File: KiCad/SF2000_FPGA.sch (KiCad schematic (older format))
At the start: 20 parts, among them J10 Conn_02x01, J11 Conn_02x01, J12 Conn_01x01, J13 Conn_02x01, J3 Conn_02x03_Odd_Even, J4 Conn_02x01, J8 Conn_02x01, J9 Conn_02x01, U3 74LVC2G14, U7 10M04SCE144

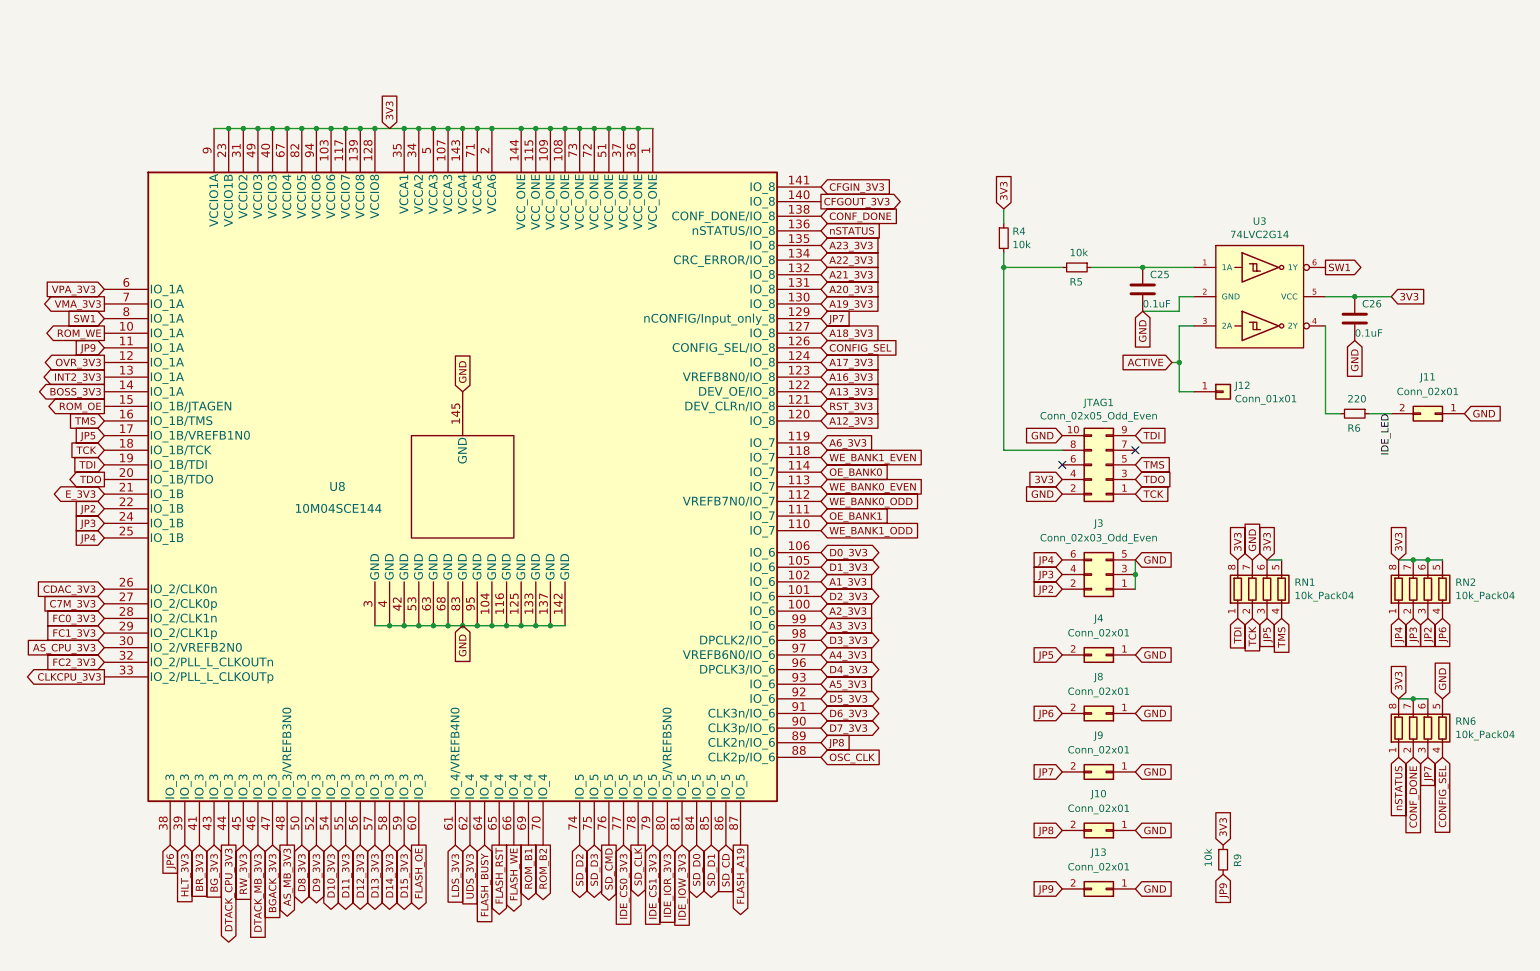
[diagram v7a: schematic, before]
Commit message: Re-routed for a GoWin FPGA GW1N-UV9LQ144 (or GW1N-UV4LQ144) and added a Pmod type 2A SPI-header.
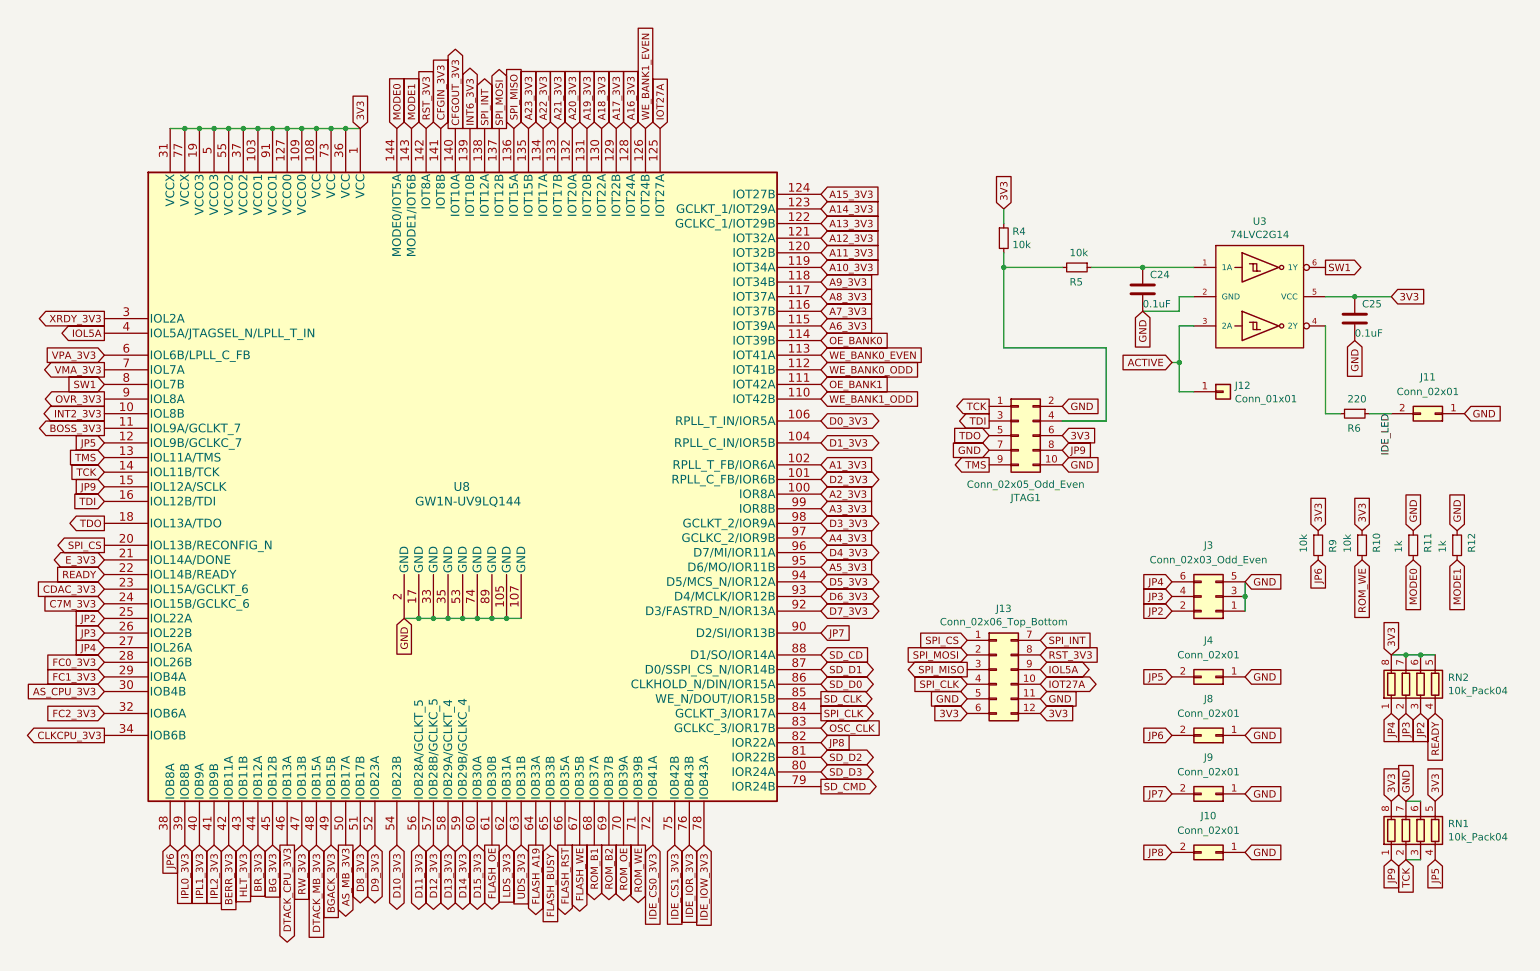
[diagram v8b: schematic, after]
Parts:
- removed J13: Conn_02x01, Connector_PinHeader_2.00mm:PinHeader_2x01_P2.00mm_Vertical, symbol Connector_Generic:Conn_02x01
- removed RN6: 10k_Pack04, SF2000:RESCAF80P320X160X60-8N, symbol Device:R_Pack04
- removed U7: 10M04SCE144, SF2000:EQFP-144-1EP_20x20mm_P0.5mm_EP5x5mm_TH_GND_pad, symbol SF2000:10M04SCE144
- added J13: Conn_02x06_Top_Bottom, SF2000:Pmod_Interface_Type_2A_SPI_PinSocket_2x06_P2.54mm_Horizontal, symbol Connector_Generic:Conn_02x06_Top_Bottom
- added R10: 10k, Resistor_SMD:R_0805_2012Metric_Pad1.15x1.40mm_HandSolder, symbol Device:R_Small
- added R11, R12: 1k, Resistor_SMD:R_0805_2012Metric_Pad1.15x1.40mm_HandSolder, symbol Device:R_Small
- added U8: GW1N-UV9LQ144, Package_QFP:LQFP-144_20x20mm_P0.5mm, symbol SF2000:GW1N-UV9LQ144
- renumbered C25 to C24, C26 to C25
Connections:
- net 3V3: now also JTAG1.6 (Pin_6), J13.12 (Pin_12), J13.6 (Pin_6), R10.1, U8.1 (VCC), U8.103 (VCCO1), U8.108 (VCC), U8.109 (VCCO0), U8.127 (VCCO0), U8.19 (VCCO3), U8.31 (VCCX), U8.36 (VCC), U8.37 (VCCO2), U8.5 (VCCO3), U8.55 (VCCO2), U8.73 (VCC), U8.77 (VCCX), U8.91 (VCCO1); no longer JTAG1.4 (Pin_4), RN1.6 (R3.2)
- net A12_3V3: now also U8.121 (IOT32A)
- net A13_3V3: now also U8.122 (GCLKC_1/IOT29B)
- net A16_3V3: now also U8.128 (IOT24A)
- net A17_3V3: now also U8.129 (IOT22B)
- net A18_3V3: now also U8.130 (IOT22A)
- net A19_3V3: now also U8.131 (IOT20B)
- net A1_3V3: now also U8.102 (RPLL_T_FB/IOR6A)
- net A20_3V3: now also U8.132 (IOT20A)
- net A21_3V3: now also U8.133 (IOT17B)
- net A22_3V3: now also U8.134 (IOT17A)
- net A23_3V3: now also U8.135 (IOT15B)
- net A2_3V3: now also U8.100 (IOR8A)
- net A3_3V3: now also U8.99 (IOR8B)
- net A4_3V3: now also U8.97 (GCLKC_2/IOR9B)
- net A5_3V3: now also U8.95 (D6/MO/IOR11B)
- net A6_3V3: now also U8.115 (IOT39A)
- net AS_CPU_3V3: now also U8.30 (IOB4B)
- net AS_MB_3V3: now also U8.50 (IOB17A)
- net BGACK_3V3: now also U8.49 (IOB15B)
- net BG_3V3: now also U8.45 (IOB12B)
- net BOSS_3V3: now also U8.11 (IOL9A/GCLKT_7)
- net BR_3V3: now also U8.44 (IOB12A)
- net C7M_3V3: now also U8.24 (IOL15B/GCLKC_6)
- net CDAC_3V3: now also U8.23 (IOL15A/GCLKT_6)
- net CFGIN_3V3: now also U8.141 (IOT8B)
- net CFGOUT_3V3: now also U8.140 (IOT10A)
- net CLKCPU_3V3: now also U8.34 (IOB6B)
- net D0_3V3: now also U8.106 (RPLL_T_IN/IOR5A)
- net D10_3V3: now also U8.54 (IOB23B)
- net D11_3V3: now also U8.56 (IOB28A/GCLKT_5)
- net D12_3V3: now also U8.57 (IOB28B/GCLKC_5)
- net D13_3V3: now also U8.58 (IOB29A/GCLKT_4)
- net D14_3V3: now also U8.59 (IOB29B/GCLKC_4)
- net D15_3V3: now also U8.60 (IOB30A)
- net D1_3V3: now also U8.104 (RPLL_C_IN/IOR5B)
- net D2_3V3: now also U8.101 (RPLL_C_FB/IOR6B)
- net D3_3V3: now also U8.98 (GCLKT_2/IOR9A)
- net D4_3V3: now also U8.96 (D7/MI/IOR11A)
- net D5_3V3: now also U8.94 (D5/MCS_N/IOR12A)
- net D6_3V3: now also U8.93 (D4/MCLK/IOR12B)
- net D7_3V3: now also U8.92 (D3/FASTRD_N/IOR13A)
- net D8_3V3: now also U8.51 (IOB17B)
- net D9_3V3: now also U8.52 (IOB23A)
- net DTACK_CPU_3V3: now also U8.46 (IOB13A)
- net DTACK_MB_3V3: now also U8.48 (IOB15A)
- net E_3V3: now also U8.21 (IOL14A/DONE)
- net FC0_3V3: now also U8.28 (IOL26B)
- net FC1_3V3: now also U8.29 (IOB4A)
- net FC2_3V3: now also U8.32 (IOB6A)
- net FLASH_A19: now also U8.64 (IOB33A)
- net FLASH_BUSY: now also U8.65 (IOB33B)
- net FLASH_OE: now also U8.61 (IOB30B)
- net FLASH_RST: now also U8.66 (IOB35A)
- net FLASH_WE: now also U8.67 (IOB35B)
- net GND: now also JTAG1.7 (Pin_7), RN1.6 (R3.2), J13.11 (Pin_11), J13.5 (Pin_5), R11.1, R12.1, U8.105 (GND), U8.107 (GND), U8.17 (GND), U8.2 (GND), U8.33 (GND), U8.35 (GND), U8.53 (GND), U8.74 (GND), U8.89 (GND)
- net HLT_3V3: now also U8.43 (IOB11B)
- net IDE_CS0_3V3: now also U8.72 (IOB41A)
- net IDE_CS1_3V3: now also U8.75 (IOB42B)
- net IDE_IOR_3V3: now also U8.76 (IOB43B)
- net IDE_IOW_3V3: now also U8.78 (IOB43A)
- net INT2_3V3: now also U8.10 (IOL8B)
- net JP2: now also U8.25 (IOL22A)
- net JP3: now also U8.26 (IOL22B)
- net JP4: now also U8.27 (IOL26A)
- net JP5: now also RN1.4 (R4.1), U8.12 (IOL9B/GCLKC_7); no longer RN1.3 (R3.1)
- net JP6: now also R9.2, U8.38 (IOB8A); no longer RN2.4 (R4.1)
- net JP7: now also U8.90 (D2/SI/IOR13B)
- net JP8: now also U8.82 (IOR22A)
- net JP9: now also JTAG1.8 (Pin_8), RN1.1 (R1.1), U8.15 (IOL12A/SCLK); no longer R9.2
- net LDS_3V3: now also U8.62 (IOB31A)
- net OE_BANK0: now also U8.114 (IOT39B)
- net OE_BANK1: now also U8.111 (IOT42A)
- net OSC_CLK: now also U8.83 (GCLKC_3/IOR17B)
- net OVR_3V3: now also U8.9 (IOL8A)
- net ROM_B1: now also U8.68 (IOB37A)
- net ROM_B2: now also U8.69 (IOB37B)
- net ROM_OE: now also U8.70 (IOB39A)
- net ROM_WE: now also R10.2, U8.71 (IOB39B)
- net RST_3V3: now also J13.8 (Pin_8), U8.142 (IOT8A)
- net RW_3V3: now also U8.47 (IOB13B)
- net SD_CD: now also U8.88 (D1/SO/IOR14A)
- net SD_CLK: now also U8.85 (WE_N/DOUT/IOR15B)
- net SD_CMD: now also U8.79 (IOR24B)
- net SD_D0: now also U8.86 (CLKHOLD_N/DIN/IOR15A)
- net SD_D1: now also U8.87 (D0/SSPI_CS_N/IOR14B)
- net SD_D2: now also U8.81 (IOR22B)
- net SD_D3: now also U8.80 (IOR24A)
- net SW1: now also U8.8 (IOL7B)
- net TCK: now also RN1.3 (R3.1), U8.14 (IOL11B/TCK)
- net TDI: now also JTAG1.3 (Pin_3), U8.16 (IOL12B/TDI); no longer JTAG1.9 (Pin_9), RN1.1 (R1.1)
- net TDO: now also JTAG1.5 (Pin_5), U8.18 (IOL13A/TDO); no longer JTAG1.3 (Pin_3)
- net TMS: now also JTAG1.9 (Pin_9), U8.13 (IOL11A/TMS); no longer JTAG1.5 (Pin_5), RN1.4 (R4.1)
- net UDS_3V3: now also U8.63 (IOB31B)
- net VMA_3V3: now also U8.7 (IOL7A)
- net VPA_3V3: now also U8.6 (IOL6B/LPLL_C_FB)
- net WE_BANK0_EVEN: now also U8.113 (IOT41A)
- net WE_BANK0_ODD: now also U8.112 (IOT41B)
- net WE_BANK1_EVEN: now also U8.126 (IOT24B)
- net WE_BANK1_ODD: now also U8.110 (IOT42B)
- net at R4.2, R5.2: now also JTAG1.4 (Pin_4); no longer JTAG1.8 (Pin_8)
- new net A10_3V3: U8.119 (IOT34A)
- new net A11_3V3: U8.120 (IOT32B)
- new net A14_3V3: U8.123 (GCLKT_1/IOT29A)
- new net A15_3V3: U8.124 (IOT27B)
- new net A7_3V3: U8.116 (IOT37B)
- new net A8_3V3: U8.117 (IOT37A)
- new net A9_3V3: U8.118 (IOT34B)
- new net BERR_3V3: U8.42 (IOB11A)
- new net INT6_3V3: U8.139 (IOT10B)
- new net IOL5A: J13.9 (Pin_9), U8.4 (IOL5A/JTAGSEL_N/LPLL_T_IN)
- new net IOT27A: J13.10 (Pin_10), U8.125 (IOT27A)
- new net IPL0_3V3: U8.39 (IOB8B)
- new net IPL1_3V3: U8.40 (IOB9A)
- new net IPL2_3V3: U8.41 (IOB9B)
- new net MODE0: R11.2, U8.144 (MODE0/IOT5A)
- new net MODE1: R12.2, U8.143 (MODE1/IOT6B)
- new net READY: RN2.4 (R4.1), U8.22 (IOL14B/READY)
- new net SPI_CLK: J13.4 (Pin_4), U8.84 (GCLKT_3/IOR17A)
- new net SPI_CS: J13.1 (Pin_1), U8.20 (IOL13B/RECONFIG_N)
- new net SPI_INT: J13.7 (Pin_7), U8.138 (IOT12A)
- new net SPI_MISO: J13.3 (Pin_3), U8.136 (IOT15A)
- new net SPI_MOSI: J13.2 (Pin_2), U8.137 (IOT12B)
- new net XRDY_3V3: U8.3 (IOL2A)
- no-connect marks 2 -> 0
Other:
- moved on the sheet: J10, J3, J4, J8, J9, JTAG1, R9, RN1, RN2
